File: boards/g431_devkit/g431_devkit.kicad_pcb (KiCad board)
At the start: 2 copper layers, 40.4 x 28.8 mm, 18 parts, among them J1 samtec_ftsh_107_01_l_dv_k, J1 usb_c_16p, U1 VAL**, U1 ht7333

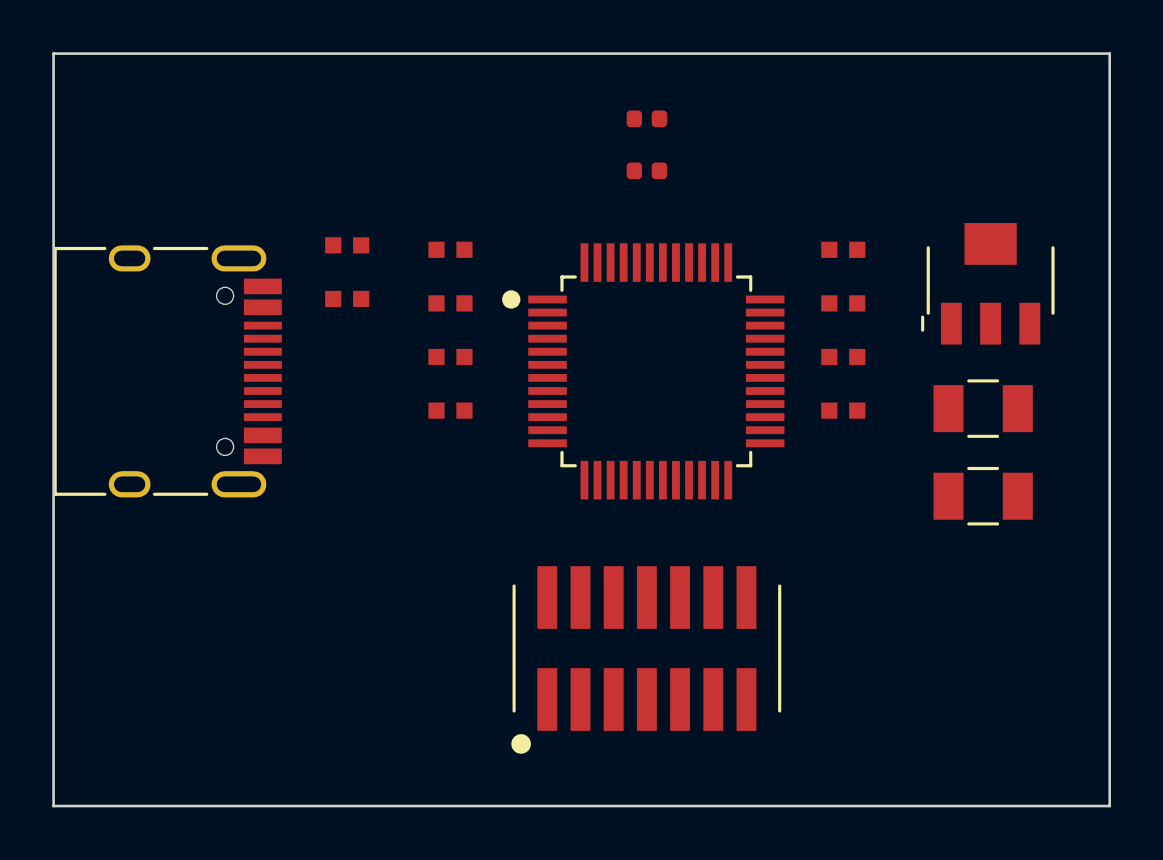
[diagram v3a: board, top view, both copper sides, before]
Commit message: P8: 부품은 물린 MCU 핀이 나오는 변에 (핀 방향 투표 배치)
- MCU 패드의 변(좌/우/상/하)을 네트별로 기록, 군집이 공유하는 신호
  네트(전원 제외)로 변 투표 — USB는 PA11/12가 있는 오른쪽 변으로 이동
  (기존 왼쪽 고정은 배선이 보드를 횡단), STDC14/I2C는 위 변(SWD·I2C 핀).
- 가장자리 회전 일반화 (face_rotation: 4변 대응), 실크=외곽 스냅도 변별.
- 가장자리 군집의 소형 부품이 부품 뒤(보드 밖)로 감기던 것 수정 —
  가장자리 부품을 최외곽 열로 정렬, 구리(패드) 외곽 이탈 0 기계 확인.
- 신호 연고 없는 군집(LDO)은 빈 변 배정. 외곽 40x25mm. DRC 0.

Co-Authored-By: Claude Fable 5 <noreply@anthropic.com>
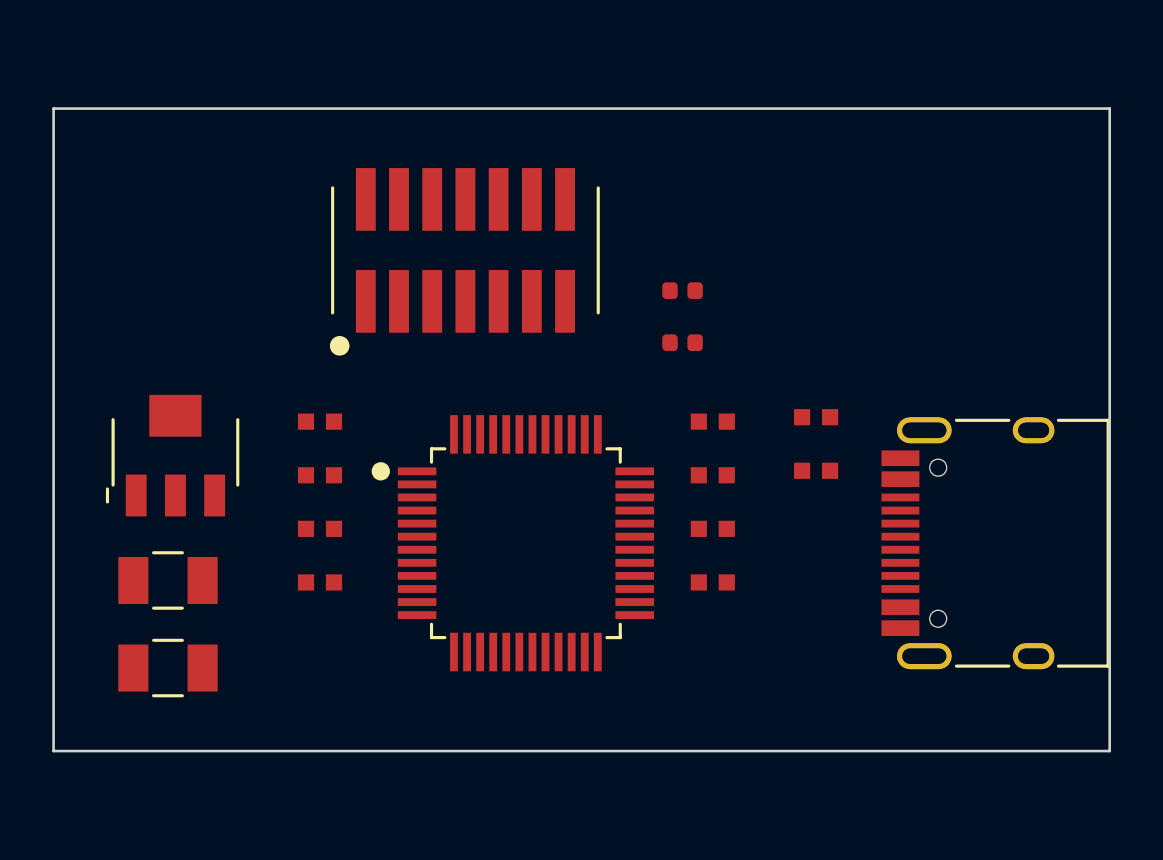
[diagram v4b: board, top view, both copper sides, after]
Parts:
- removed the C1 at (163.9, 104.2)
- removed the C1 at (158.5, 98.1)
- removed the C2 at (143.5, 98.1)
- removed the C2 at (163.9, 107.5)
- removed the J1 at (132.3, 102.8)
- removed the J1 at (151.0, 113.4)
- removed the R1 at (151.0, 93.1)
- removed the R1 at (143.5, 104.3)
- removed the R1 at (139.5, 97.9)
- removed the R2 at (151.0, 95.1)
- removed the R2 at (139.5, 100.0)
- removed the U1 at (164.1, 99.3)
- removed the U1 at (151.4, 102.8)
- added C1: VAL**, antmicro_cl05a104ka5nnnc, F.Cu at (153.5, 104.7)
- added C1: VAL**, antmicro_c3216x7r1h106k160ae, F.Cu at (132.7, 110.8)
- added C2: VAL**, antmicro_cl05a104ka5nnnc, F.Cu at (138.5, 104.7)
- added C2: VAL**, antmicro_c3216x7r1h106k160ae, F.Cu at (132.7, 114.1)
- added J1: samtec_ftsh_107_01_l_dv_k, samtec_ftsh_107_01_l_dv_k, F.Cu at (144.1, 98.1)
- added J1: usb_c_16p, usb_c_16p, F.Cu at (164.7, 109.3)
- added R1: R_0402_1005Metric, antmicro_crcw04021k80fkedc, F.Cu at (152.4, 99.7)
- added R1: VAL**, vishay_crcw04025k10fked, F.Cu at (157.5, 104.5)
- added R1: VAL**, vishay_crcw040210k0fked, F.Cu at (138.5, 110.8)
- added R2: VAL**, vishay_crcw04025k10fked, F.Cu at (157.5, 106.6)
- added R2: R_0402_1005Metric, antmicro_crcw04021k80fkedc, F.Cu at (152.4, 101.7)
- added U1: ht7333, ht7333, F.Cu at (133.0, 105.9)
- added U1: VAL**, stm32g431cbtx, F.Cu at (146.4, 109.3)
- moved C3 8.25 mm to (153.5, 106.7)
- moved C4 8.25 mm to (138.5, 106.7)
- moved C5 8.25 mm to (153.5, 108.8)
- moved C6 8.25 mm to (138.5, 108.8)
- moved C7 8.25 mm to (153.5, 110.8)
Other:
- board size 40.4 x 28.8 mm -> 40.4 x 24.6 mm

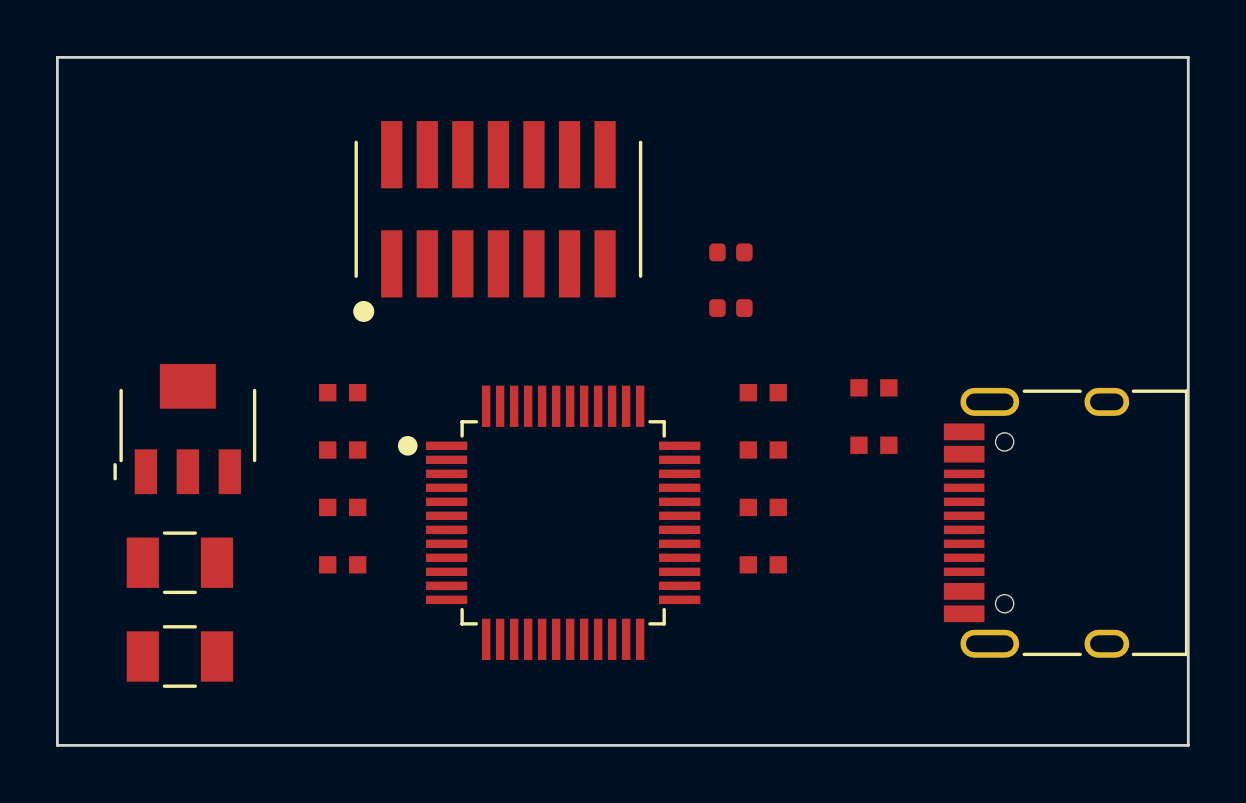
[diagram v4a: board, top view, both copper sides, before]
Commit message: P9~P11: 신호 위주 배치·꼬임 최소·선폭 간격 (외곽 39x24)
- P9: 전원/GND는 배치 고려 제외 — 전원 전용 부품은 좌우 잔여 공간 채움
- P10: 신호 부품은 물린 MCU 핀의 변에, 핀 y 순서대로 (군집도 같은 변에서
  핀 좌표순 정렬) — 랫츠네스트 꼬임 방지
- P11: 부품 간격 1.0 -> 0.6mm (트레이스 1가닥+클리어런스)
- DRC 0 유지, 사용자 원문 규칙집 기록

Co-Authored-By: Claude Fable 5 <noreply@anthropic.com>
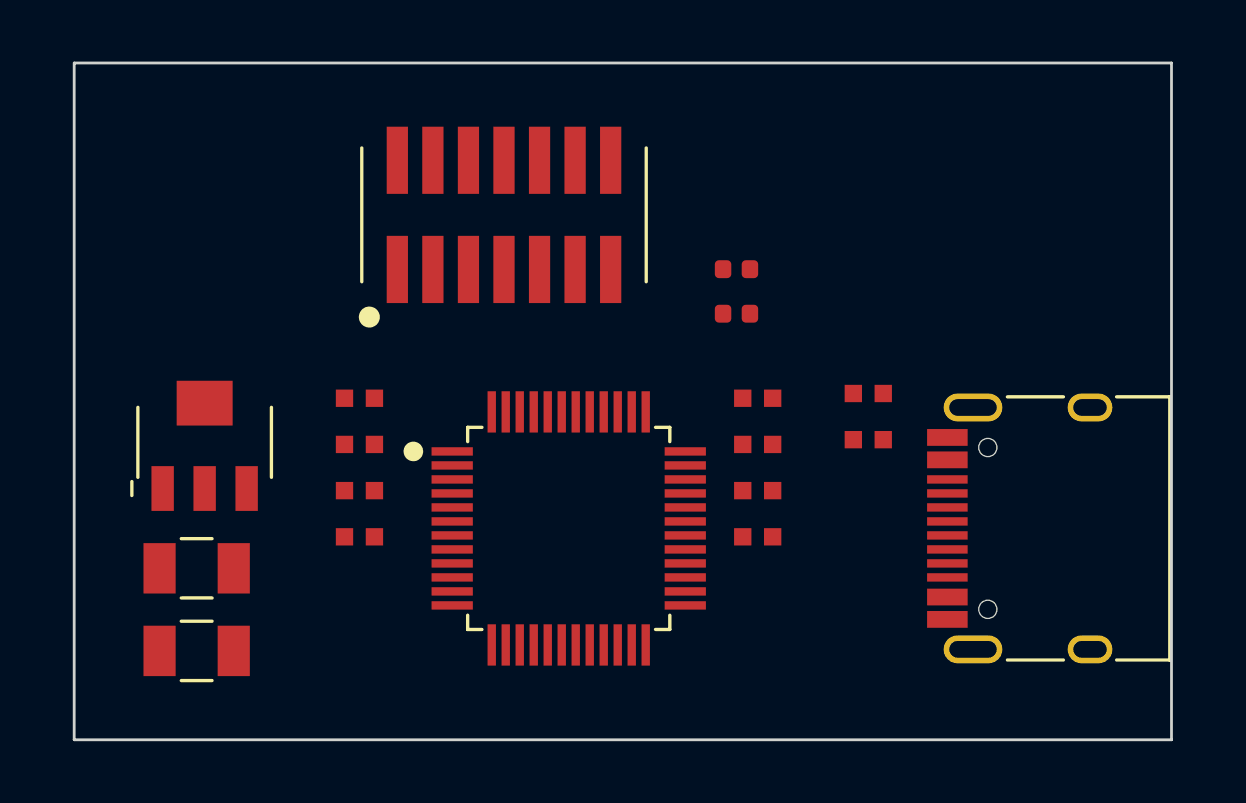
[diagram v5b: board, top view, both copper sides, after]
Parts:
- removed the C1 at (153.5, 104.7)
- removed the C1 at (132.7, 110.8)
- removed the C2 at (138.5, 104.7)
- removed the C2 at (132.7, 114.1)
- removed the J1 at (144.1, 98.1)
- removed the J1 at (164.7, 109.3)
- removed the R1 at (152.4, 99.7)
- removed the R1 at (157.5, 104.5)
- removed the R1 at (138.5, 110.8)
- removed the R2 at (157.5, 106.6)
- removed the R2 at (152.4, 101.7)
- removed the U1 at (133.0, 105.9)
- removed the U1 at (146.4, 109.3)
- added C1: VAL**, antmicro_c3216x7r1h106k160ae, F.Cu at (133.3, 111.0)
- added C1: VAL**, antmicro_cl05a104ka5nnnc, F.Cu at (153.3, 104.9)
- added C2: VAL**, antmicro_c3216x7r1h106k160ae, F.Cu at (133.3, 113.9)
- added C2: VAL**, antmicro_cl05a104ka5nnnc, F.Cu at (153.3, 106.5)
- added J1: samtec_ftsh_107_01_l_dv_k, samtec_ftsh_107_01_l_dv_k, F.Cu at (144.3, 98.3)
- added J1: usb_c_16p, usb_c_16p, F.Cu at (164.1, 109.5)
- added R1: VAL**, vishay_crcw04025k10fked, F.Cu at (157.3, 104.7)
- added R1: VAL**, vishay_crcw040210k0fked, F.Cu at (139.1, 104.9)
- added R1: R_0402_1005Metric, antmicro_crcw04021k80fkedc, F.Cu at (152.6, 100.3)
- added R2: R_0402_1005Metric, antmicro_crcw04021k80fkedc, F.Cu at (152.6, 101.9)
- added R2: VAL**, vishay_crcw04025k10fked, F.Cu at (157.3, 106.4)
- added U1: ht7333, ht7333, F.Cu at (133.6, 106.5)
- added U1: VAL**, stm32g431cbtx, F.Cu at (146.6, 109.5)
- moved C7 15.1 mm to (139.1, 106.5)
- moved C4 14.9 mm to (153.3, 108.2)
- moved C6 14.9 mm to (153.3, 109.8)
- moved C3 14.5 mm to (139.1, 108.2)
- moved C5 14.5 mm to (139.1, 109.8)
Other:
- board size 40.4 x 24.6 mm -> 39.2 x 24.2 mm

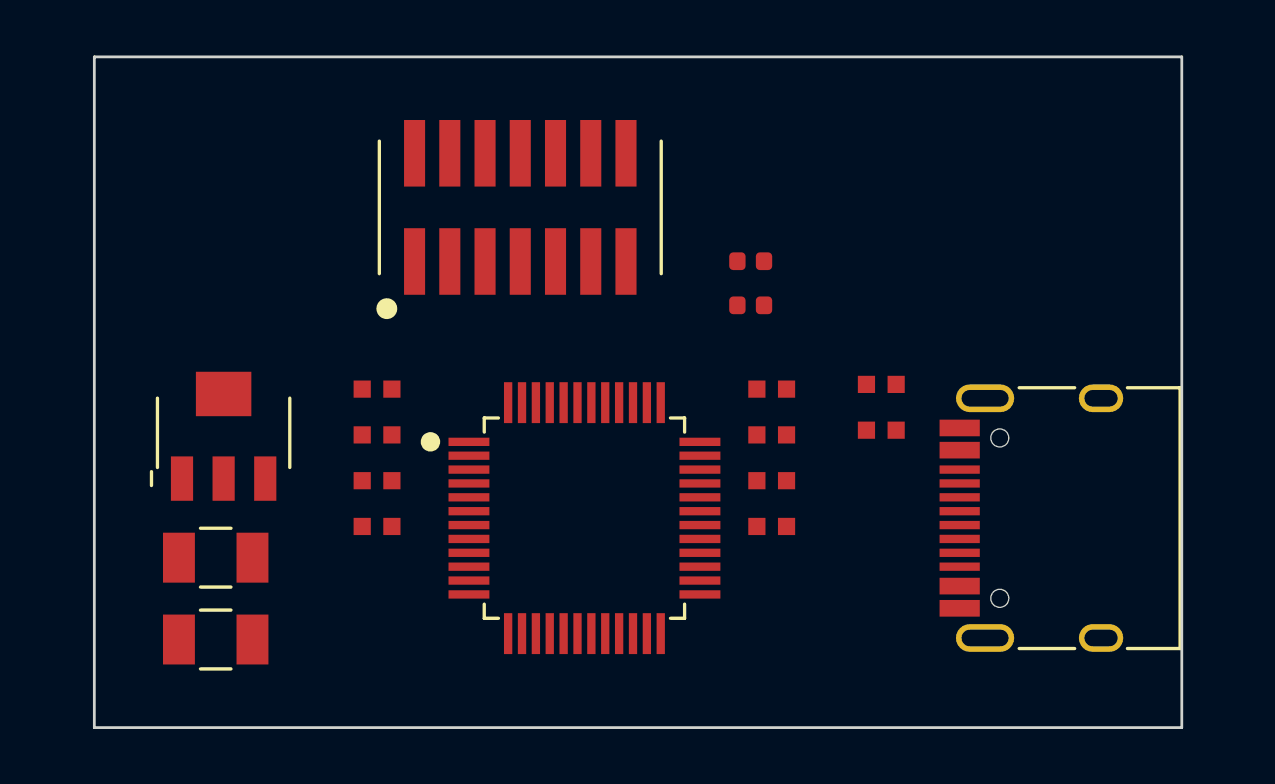
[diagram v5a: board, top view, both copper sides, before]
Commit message: P5 확정: REF는 실크에 (SMT 필수) — 옆/위 배치, 자리 예약
- 'SMT를 어떻게 치라고 그걸 빼냐' — Fab 이동안 기각. 소형 부품은 열 폭에
  REF_W(2.6mm)를 예약하고 바깥쪽 옆에 0.8mm 글자, IC/커넥터는 몸체 위.
- DRC 0 유지 (실크 REF가 패드 안 물음), 외곽 42x24mm.

Co-Authored-By: Claude Fable 5 <noreply@anthropic.com>
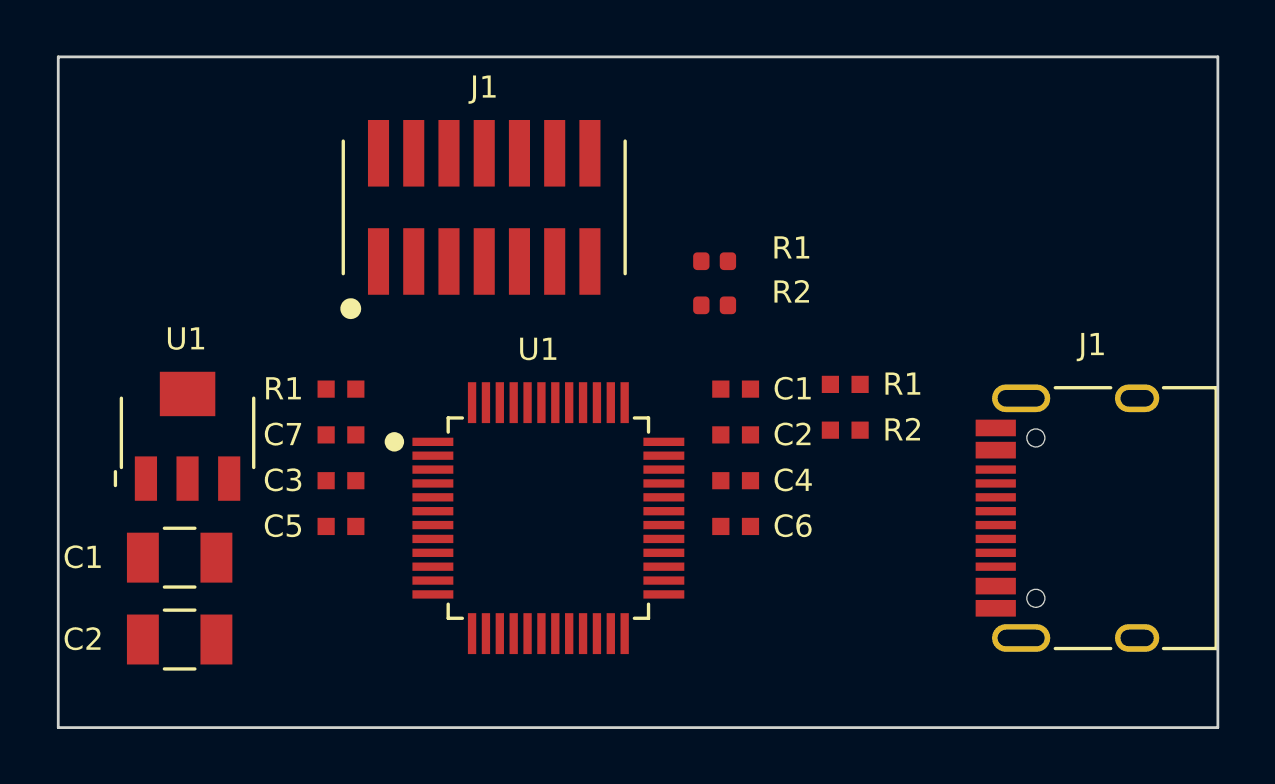
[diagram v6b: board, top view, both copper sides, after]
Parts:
- removed the C1 at (133.3, 111.0)
- removed the C1 at (153.3, 104.9)
- removed the C2 at (133.3, 113.9)
- removed the C2 at (153.3, 106.5)
- removed the J1 at (144.3, 98.3)
- removed the J1 at (164.1, 109.5)
- removed the R1 at (157.3, 104.7)
- removed the R1 at (139.1, 104.9)
- removed the R1 at (152.6, 100.3)
- removed the R2 at (152.6, 101.9)
- removed the R2 at (157.3, 106.4)
- removed the U1 at (133.6, 106.5)
- removed the U1 at (146.6, 109.5)
- added C1: VAL**, antmicro_c3216x7r1h106k160ae, F.Cu at (132.0, 111.0)
- added C1: VAL**, antmicro_cl05a104ka5nnnc, F.Cu at (152.0, 104.9)
- added C2: VAL**, antmicro_c3216x7r1h106k160ae, F.Cu at (132.0, 113.9)
- added C2: VAL**, antmicro_cl05a104ka5nnnc, F.Cu at (152.0, 106.5)
- added J1: samtec_ftsh_107_01_l_dv_k, samtec_ftsh_107_01_l_dv_k, F.Cu at (143.0, 98.3)
- added J1: usb_c_16p, usb_c_16p, F.Cu at (165.4, 109.5)
- added R1: R_0402_1005Metric, antmicro_crcw04021k80fkedc, F.Cu at (151.3, 100.3)
- added R1: VAL**, vishay_crcw04025k10fked, F.Cu at (156.0, 104.7)
- added R1: VAL**, vishay_crcw040210k0fked, F.Cu at (137.8, 104.9)
- added R2: VAL**, vishay_crcw04025k10fked, F.Cu at (156.0, 106.4)
- added R2: R_0402_1005Metric, antmicro_crcw04021k80fkedc, F.Cu at (151.3, 101.9)
- added U1: VAL**, stm32g431cbtx, F.Cu at (145.3, 109.5)
- added U1: ht7333, ht7333, F.Cu at (132.3, 106.5)
- moved C3 1.30 mm to (137.8, 108.2)
- moved C4 1.30 mm to (152.0, 108.2)
- moved C5 1.30 mm to (137.8, 109.8)
- moved C6 1.30 mm to (152.0, 109.8)
- moved C7 1.30 mm to (137.8, 106.5)
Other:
- board size 39.2 x 24.2 mm -> 41.8 x 24.2 mm

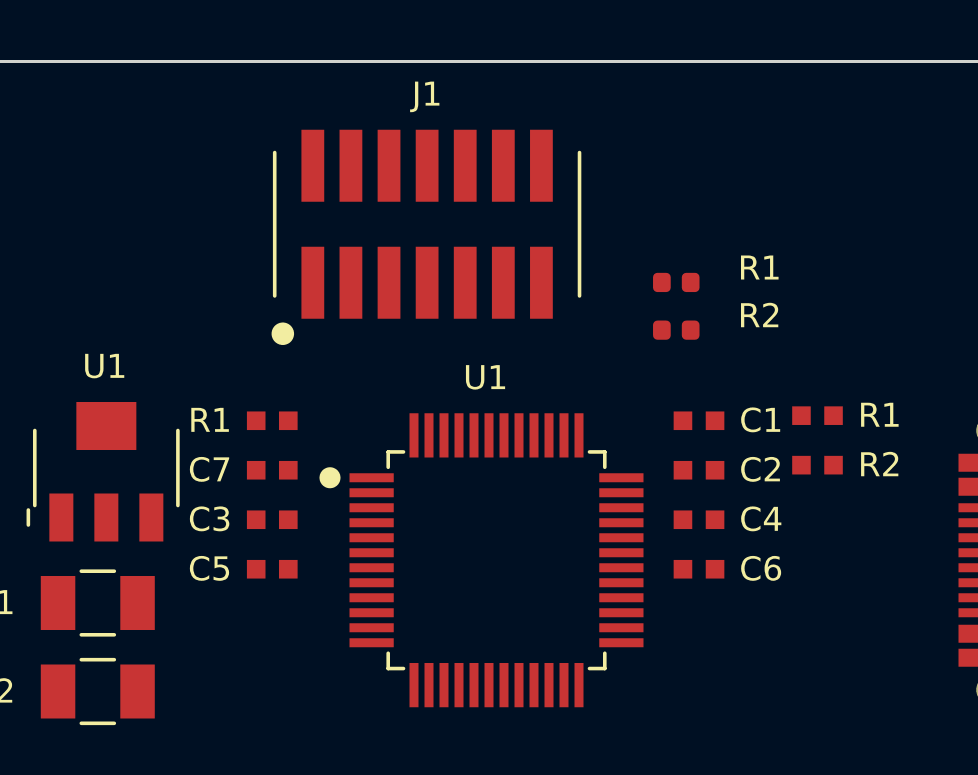
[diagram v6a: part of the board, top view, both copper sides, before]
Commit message: 보드 전역 주석(annotate): 블록 인스턴스별 사본 + 고유 참조번호
- 블록 조합의 참조 중복(U1x2, J1x2 — SMT 작업지시 불가) 해소: build_board가
  블록 sch를 보드 폴더에 인스턴스별 사본으로 넣고 KiCad 계층 주석 방식
  (instances 블록 교체)으로 전역 번호 부여 (U1/U2, J1/J2, C1~C9, R1~R5,
  #PWR/#FLG 포함). R12 자유 텍스트 표기 동기화.
- 보드 폴더 자립형화 (Sheetfile 로컬 — 키캐드/test 복사도 통째로).
- ref_map.json 산출, check_board 넷 대조가 지도 반영. 전 게이트 통과.

Co-Authored-By: Claude Fable 5 <noreply@anthropic.com>
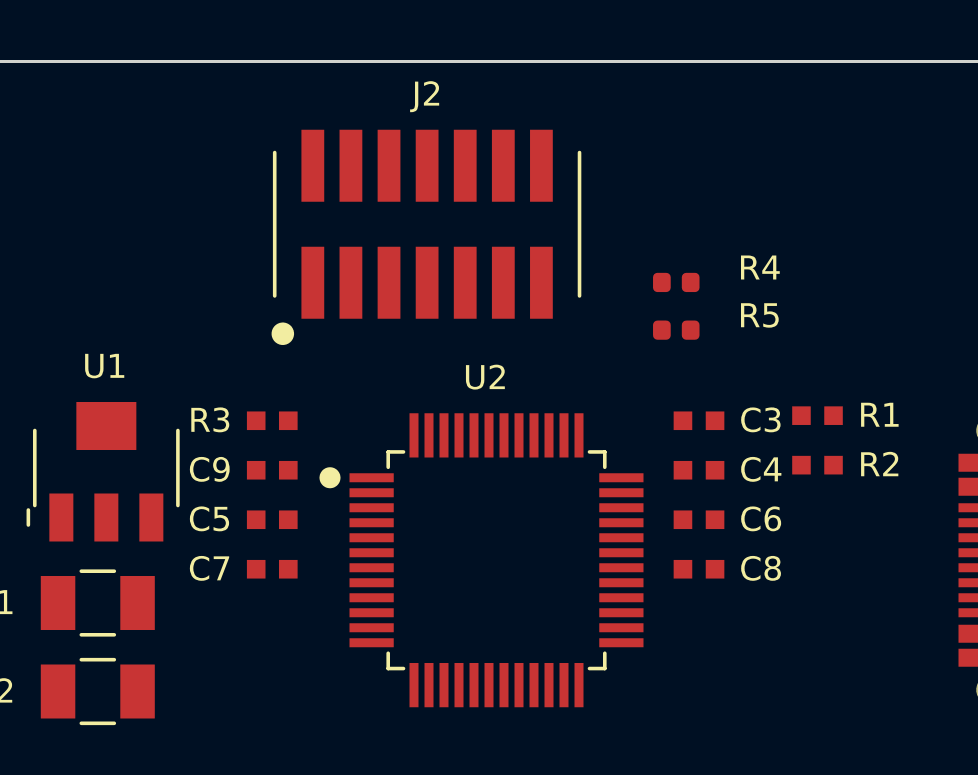
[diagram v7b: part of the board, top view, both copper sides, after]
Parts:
- removed the C1 at (152.0, 104.9)
- removed the C2 at (152.0, 106.5)
- removed the J1 at (143.0, 98.3)
- removed the R1 at (151.3, 100.3)
- removed the R1 at (137.8, 104.9)
- removed the R2 at (151.3, 101.9)
- removed the U1 at (145.3, 109.5)
- added C8: VAL**, samsung_cl05a105ka5nnnc, F.Cu at (152.0, 109.8)
- added C9: VAL**, antmicro_cl05a104ka5nnnc, F.Cu at (137.8, 106.5)
- added J2: samtec_ftsh_107_01_l_dv_k, samtec_ftsh_107_01_l_dv_k, F.Cu at (143.0, 98.3)
- added R3: VAL**, vishay_crcw040210k0fked, F.Cu at (137.8, 104.9)
- added R4: R_0402_1005Metric, antmicro_crcw04021k80fkedc, F.Cu at (151.3, 100.3)
- added R5: R_0402_1005Metric, antmicro_crcw04021k80fkedc, F.Cu at (151.3, 101.9)
- added U2: VAL**, stm32g431cbtx, F.Cu at (145.3, 109.5)
- C4: footprint antmicro_cl05a475kq5nrnc -> antmicro_cl05a104ka5nnnc
- C6: footprint samsung_cl05a105ka5nnnc -> antmicro_cl05a475kq5nrnc
- moved C3 14.6 mm to (152.0, 104.9)
- moved C7 3.30 mm to (137.8, 109.8)
- moved C4 1.65 mm to (152.0, 106.5)
- moved C5 1.65 mm to (137.8, 108.2)
- moved C6 1.65 mm to (152.0, 108.2)
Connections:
- C7 pad 2: NRST -> +3V3
- R1 pad 1: SDA -> GND
- R2 pad 1: SCL -> GND
- U1 pad 2: /B3 g431_min/PC13 -> +5V
- U1 pad 3: /B3 g431_min/PC14-OSC32_IN -> +3V3
